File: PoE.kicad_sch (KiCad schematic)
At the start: 24 parts, among them IC1 TPS2378DDA

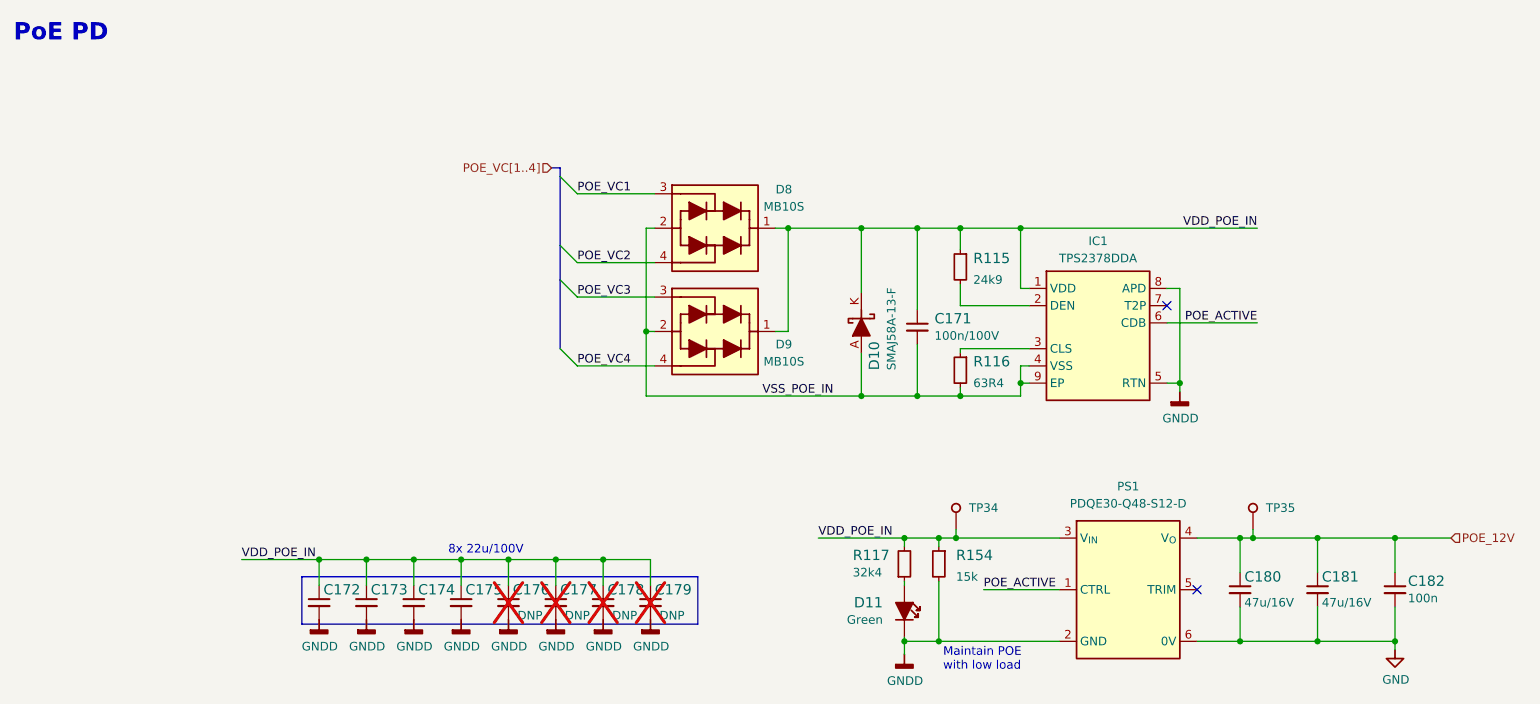
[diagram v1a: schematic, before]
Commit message: Certain components deleted
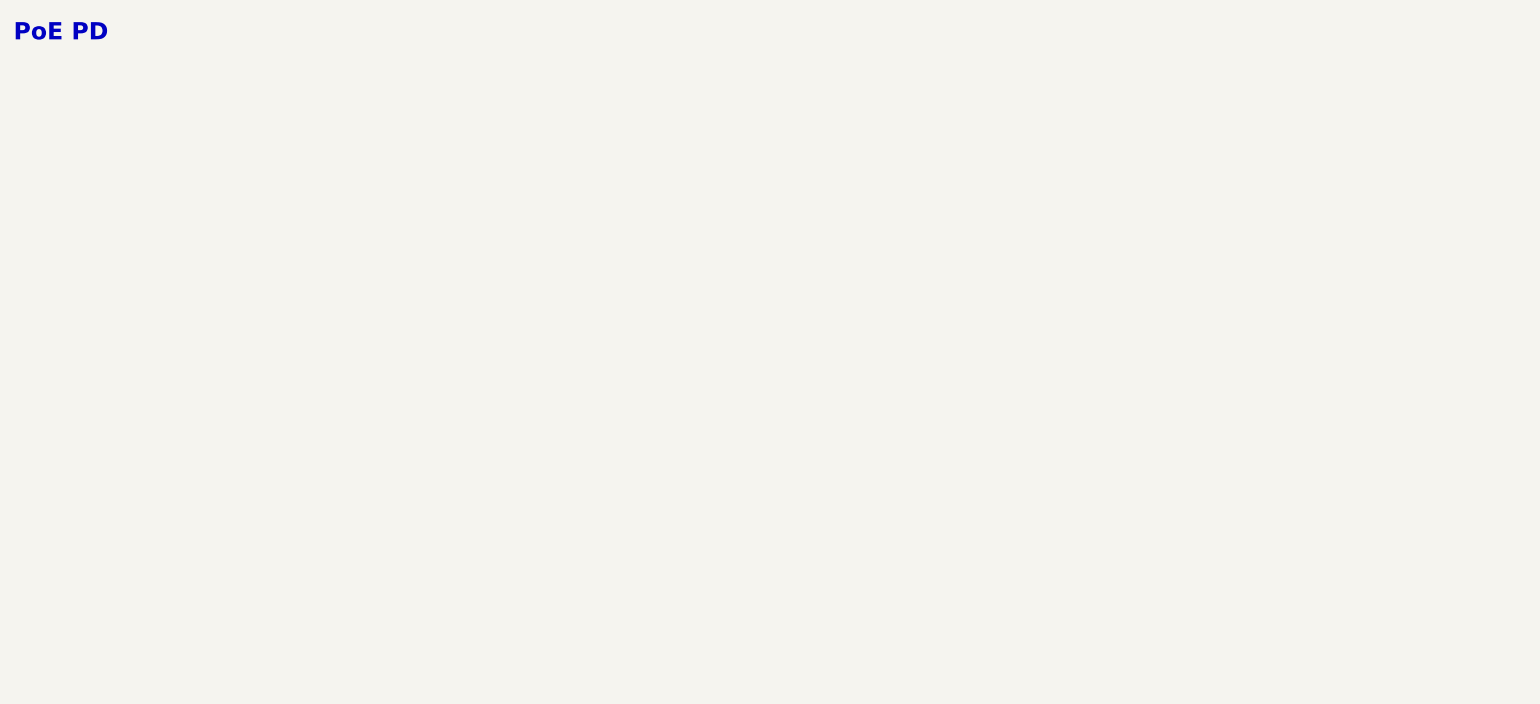
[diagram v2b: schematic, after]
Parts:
- removed C171: C_100n_0805_100V, kria-k26-devboard-footprints:C_0805_2012Metric, symbol kria-k26-devboard:C_100n_100V_0805
- removed C172, C173, C174, C175, C176, C177, C178, C179: C_22u_100V_2220, kria-k26-devboard-footprints:C_2220_5650Metric, symbol kria-k26-devboard:C_22u_100V_2220
- removed C180, C181: C_47u_16V_1206, kria-k26-devboard-footprints:C_1206_3216Metric, symbol kria-k26-devboard:C_47u_16V_1206
- removed C182: C_100n_0402, kria-k26-devboard-footprints:C_0402_1005Metric, symbol kria-k26-devboard:C_100n_0402
- removed D10: SMAJ58A-13-F, kria-k26-devboard-footprints:DO-214AC, symbol kria-k26-devboard:SMAJ58A-13-F
- removed D11: LED_G_0603_LG_L29K-G2J1-24-Z, kria-k26-devboard-footprints:LED_0603_1608Metric_G, symbol kria-k26-devboard:LED_G_0603_LG_L29K-G2J1-24-Z
- removed D8, D9: MB10S, kria-k26-devboard-footprints:SOIC-4_W3.9mm, symbol kria-k26-devboard:MB10S
- removed IC1: TPS2378DDA, kria-k26-devboard-footprints:SOIC-8-1EP_3.9x4.9x1.75mm_P1.27mm, symbol kria-k26-devboard:TPS2378DDA
- removed PS1: PDQE30-Q48-S12-D, kria-k26-devboard-footprints:CONV_PDQE30-Q48-S5-D, symbol kria-k26-devboard:PDQE30-Q48-S12-D
- removed R115: R_24k9_0402, kria-k26-devboard-footprints:R_0402_1005Metric, symbol kria-k26-devboard:R_24k9_0402
- removed R116: R_63R4_0603, kria-k26-devboard-footprints:R_0603_1608Metric, symbol kria-k26-devboard:R_63R4_0603
- removed R117: R_32k4_0805, kria-k26-devboard-footprints:R_0805_2012Metric, symbol kria-k26-devboard:R_32k4_0805
- removed R154: R_15k_2010, kria-k26-devboard-footprints:R_2010_5025Metric, symbol kria-k26-devboard:R_15k_2010
- removed TP34, TP35: TP_0.75mm_SMD, kria-k26-devboard-footprints:TP_SMD_0.75mm, symbol kria-k26-devboard:TP_0.75mm_SMD
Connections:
- no-connect marks 2 -> 0
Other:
- note removed: "8x 22u/100V"
- note removed: "Maintain POE with low load"
